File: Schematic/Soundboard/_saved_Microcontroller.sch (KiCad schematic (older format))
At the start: 18 parts, among them J4 USB_B_Micro, J5 Conn_01x03_Male, J6 Conn_02x02_Counter_Clockwise, J7 Conn_ARM_JTAG_SWD_10, SW1 SW_Push, U1 STM32f429IIT6-units, U9 USBLC6-4SC6, Y1 Crystal_GND24

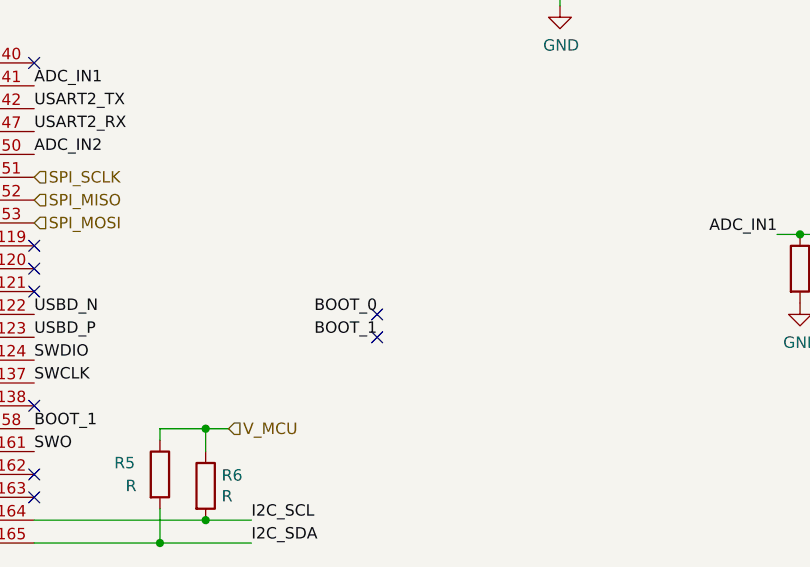
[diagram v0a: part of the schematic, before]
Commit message: Complete part selection. Start connections
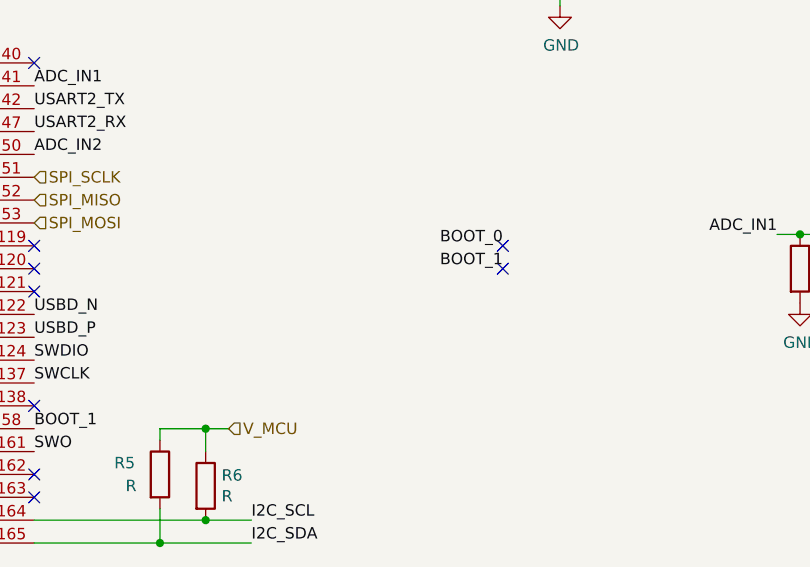
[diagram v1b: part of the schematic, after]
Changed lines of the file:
@@
 Text Label 8200 5400 0    50   ~ 0
 I2C_SDA
-Text Label 5450 3200 2    50   ~ 0
+Text Label 6000 2900 2    50   ~ 0
 BOOT_0
-Text Label 5450 3300 2    50   ~ 0
+Text Label 6000 3000 2    50   ~ 0
 BOOT_1
-NoConn ~ 5450 3300
-NoConn ~ 5450 3200
+NoConn ~ 6000 3000
+NoConn ~ 6000 2900
 Text HLabel 7650 2850 2    50   Input ~ 0
 V_BAT
